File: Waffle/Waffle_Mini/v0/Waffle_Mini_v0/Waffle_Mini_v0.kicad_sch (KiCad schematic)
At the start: 17 parts, among them J1 cJTAG, U1 F2800154QRHBRQ1, U2 AP7375-33SA-7, X1 CSTNE20M0V530000R0

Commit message: Layout kinda done v0 waffle mini
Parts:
- removed J1: cJTAG, Connector_PinHeader_1.27mm:PinHeader_1x06_P1.27mm_Vertical_SMD_Pin1Left, symbol Connector_Generic:Conn_02x03_Odd_Even
- added J1: Conn_ARM_SWD_TagConnect_TC2030-NL, Connector:Tag-Connect_TC2030-IDC-NL_2x03_P1.27mm_Vertical, symbol Connector:Conn_ARM_SWD_TagConnect_TC2030-NL
- added J10, J11, J12, J13, J14, J15, J16, J17, J18, J19, J2, J20, J21, J22, J23, J24, J25, J26, J27, J28, J29, J3, J4, J5, J6, J7, J8, J9: Conn_01x01_Socket, ICDB_Waffle:ICDB_Castellated_Pad, symbol Connector:Conn_01x01_Socket
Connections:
- net +3.3V: now also J1.1 (VCC), J25.1 (Pin_1)
- net +VSW: now also J24.1 (Pin_1)
- net GND: now also J1.5 (GND), J15.1 (Pin_1), J16.1 (Pin_1), J26.1 (Pin_1), J27.1 (Pin_1), J28.1 (Pin_1), J29.1 (Pin_1)
- net JTAG_TCK: now also J1.4 (SWCLK)
- net JTAG_TMS: now also J1.2 (SWDIO)
- net XRSn: now also J1.3 (~{RESET})
- net at U1.12 (A4/C14): now also J10.1 (Pin_1)
- net at U1.13 (A10/C10_C8/A9_GPIO227_230): now also J11.1 (Pin_1)
- net at U1.14 (GPIO11): now also J12.1 (Pin_1)
- net at U1.15 (GPIO24): now also J13.1 (Pin_1)
- net at U1.17 (GPIO37_TDO): now also J14.1 (Pin_1)
- net at U1.2 (GPIO226_228_A6/C6): now also J2.1 (Pin_1)
- net at U1.26 (GPIO3): now also J17.1 (Pin_1)
- net at U1.27 (GPIO1): now also J18.1 (Pin_1)
- net at U1.28 (GPIO0): now also J19.1 (Pin_1)
- net at U1.29 (GPIO7): now also J20.1 (Pin_1)
- net at U1.3 (GPIO242_A3/C5): now also J3.1 (Pin_1)
- net at U1.30 (GPIO5): now also J21.1 (Pin_1)
- net at U1.31 (GPIO29): now also J22.1 (Pin_1)
- net at U1.32 (A16/C16_GPIO28): now also J23.1 (Pin_1)
- net at U1.4 (GPIO224_A2/C9): now also J4.1 (Pin_1)
- net at U1.5 (A15/C7_C4/A14): now also J5.1 (Pin_1)
- net at U1.6 (A11/C0_A5/C2): now also J6.1 (Pin_1)
- net at U1.7 (A0/C15/CMP1_DACL_A1): now also J7.1 (Pin_1)
- net at U1.8 (A12/C1_A7/C3): now also J8.1 (Pin_1)
- net at U1.9 (A8/C11): now also J9.1 (Pin_1)
- no-connect marks 0 -> 3
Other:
- moved on the sheet: R2, R3

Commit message: Curly added :)
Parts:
- added C11: 10n, Capacitor_SMD:C_0603_1608Metric, symbol Device:C_Small
- added R4: 4k7, Resistor_SMD:R_0603_1608Metric, symbol Device:R_Small_US
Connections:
- net +3.3V: now also R4.1
- net GND: now also C11.2
- net XRSn: now also C11.1, R4.2
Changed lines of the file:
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@@
   (junction (at 66.04 35.56) (diameter 0) (color 0 0 0 0)
+  )
+  (junction (at 21.59 123.19) (diameter 0) (color 0 0 0 0)
   )
   (junction (at 29.21 85.09) (diameter 0) (color 0 0 0 0)
@@
     (stroke (width 0) (type default))
   )
+  (wire (pts (xy 21.59 115.57) (xy 21.59 116.84))
+    (stroke (width 0) (type default))
+  )
   (wire (pts (xy 69.85 130.81) (xy 83.82 130.81))
     (stroke (width 0) (type default))
   )
-  (wire (pts (xy 26.67 123.19) (xy 34.29 123.19))
+  (wire (pts (xy 21.59 123.19) (xy 34.29 123.19))
     (stroke (width 0) (type default))
   )
@@
     (stroke (width 0) (type default))
   )
+  (wire (pts (xy 21.59 129.54) (xy 21.59 130.81))
+    (stroke (width 0) (type default))
+  )
   (wire (pts (xy 69.85 123.19) (xy 83.82 123.19))
     (stroke (width 0) (type default))
@@
     (stroke (width 0) (type default))
   )
+  (wire (pts (xy 21.59 123.19) (xy 21.59 124.46))
+    (stroke (width 0) (type default))
+  )
   (polyline (pts (xy 223.52 130.81) (xy 223.52 135.89))
     (stroke (width 0) (type default))
@@
   )
   (wire (pts (xy 69.85 144.78) (xy 83.82 144.78))
+    (stroke (width 0) (type default))
+  )
+  (wire (pts (xy 21.59 121.92) (xy 21.59 123.19))
     (stroke (width 0) (type default))
   )
@@
     )
   )
+  (symbol (lib_id "power:+3.3V") (at 21.59 115.57 0) (unit 1)
+    (in_bom yes) (on_board yes) (dnp no) (fields_autoplaced)
+    (property "Reference" "#PWR028" (at 21.59 119.38 0)
+      (effects (font (size 1.27 1.27)) hide)
+    )
+    (property "Value" "+3.3V" (at 21.59 110.49 0)
+      (effects (font (size 1.27 1.27)))
+    )
+    (property "Footprint" "" (at 21.59 115.57 0)
+      (effects (font (size 1.27 1.27)) hide)
+    )
+    (property "Datasheet" "" (at 21.59 115.57 0)
+      (effects (font (size 1.27 1.27)) hide)
+    )
+    (pin "1")
+    (instances
+      (project "Waffle_Mini_v0"
+        (path "/549e8335-6523-4521-9df7-6bd7c43d4ddf"
+          (reference "#PWR028") (unit 1)
+        )
+      )
+    )
+  )
   (symbol (lib_id "power:+3.3V") (at 29.21 78.74 0) (unit 1)
     (in_bom yes) (on_board yes) (dnp no) (fields_autoplaced)
@@
         (path "/549e8335-6523-4521-9df7-6bd7c43d4ddf"
           (reference "C7") (unit 1)
+        )
+      )
+    )
+  )
+  (symbol (lib_id "Device:C_Small") (at 21.59 127 0) (mirror y) (unit 1)
+    (in_bom yes) (on_board yes) (dnp no)
+    (property "Reference" "C11" (at 19.05 125.7363 0)
+      (effects (font (size 1.27 1.27)) (justify left))
+    )
+    (property "Value" "10n" (at 19.05 128.2763 0)
+      (effects (font (size 1.27 1.27)) (justify left))
+    )
+    (property "Footprint" "Capacitor_SMD:C_0603_1608Metric" (at 21.59 127 0)
+      (effects (font (size 1.27 1.27)) hide)
+    )
+    (property "Datasheet" "~" (at 21.59 127 0)
+      (effects (font (size 1.27 1.27)) hide)
+    )
+    (pin "1")
+    (pin "2")
+    (instances
+      (project "Waffle_Mini_v0"
+        (path "/549e8335-6523-4521-9df7-6bd7c43d4ddf"
+          (reference "C11") (unit 1)
         )
       )
@@
     )
   )
+  (symbol (lib_id "Device:R_Small_US") (at 21.59 119.38 0) (mirror y) (unit 1)
+    (in_bom yes) (on_board yes) (dnp no)
+    (property "Reference" "R4" (at 19.05 118.11 0)
+      (effects (font (size 1.27 1.27)) (justify left))
+    )
+    (property "Value" "4k7" (at 19.05 120.65 0)
+      (effects (font (size 1.27 1.27)) (justify left))
+    )
+    (property "Footprint" "Resistor_SMD:R_0603_1608Metric" (at 21.59 119.38 0)
+      (effects (font (size 1.27 1.27)) hide)
+    )
+    (property "Datasheet" "~" (at 21.59 119.38 0)
+      (effects (font (size 1.27 1.27)) hide)
+    )
+    (pin "1")
+    (pin "2")
+    (instances
+      (project "Waffle_Mini_v0"
+        (path "/549e8335-6523-4521-9df7-6bd7c43d4ddf"
+          (reference "R4") (unit 1)
+        )
+      )
+    )
+  )
   (symbol (lib_id "power:GND") (at 185.42 49.53 0) (unit 1)
     (in_bom yes) (on_board yes) (dnp no) (fields_autoplaced)
@@
         )
       )
+    )
+  )
+  (symbol (lib_id "power:GND") (at 21.59 130.81 0) (unit 1)
+    (in_bom yes) (on_board yes) (dnp no) (fields_autoplaced)
+    (property "Reference" "#PWR029" (at 21.59 137.16 0)
+      (effects (font (size 1.27 1.27)) hide)
+    )
+    (property "Value" "GND" (at 21.59 135.89 0)
+      (effects (font (size 1.27 1.27)))
+    )
+    (property "Footprint" "" (at 21.59 130.81 0)
+      (effects (font (size 1.27 1.27)) hide)
+    )
+    (property "Datasheet" "" (at 21.59 130.81 0)
+      (effects (font (size 1.27 1.27)) hide)
+    )
+    (pin "1")
+    (instances
+      (project "Waffle_Mini_v0"
+        (path "/549e8335-6523-4521-9df7-6bd7c43d4ddf"
+          (reference "#PWR029") (unit 1)
+        )
+      )

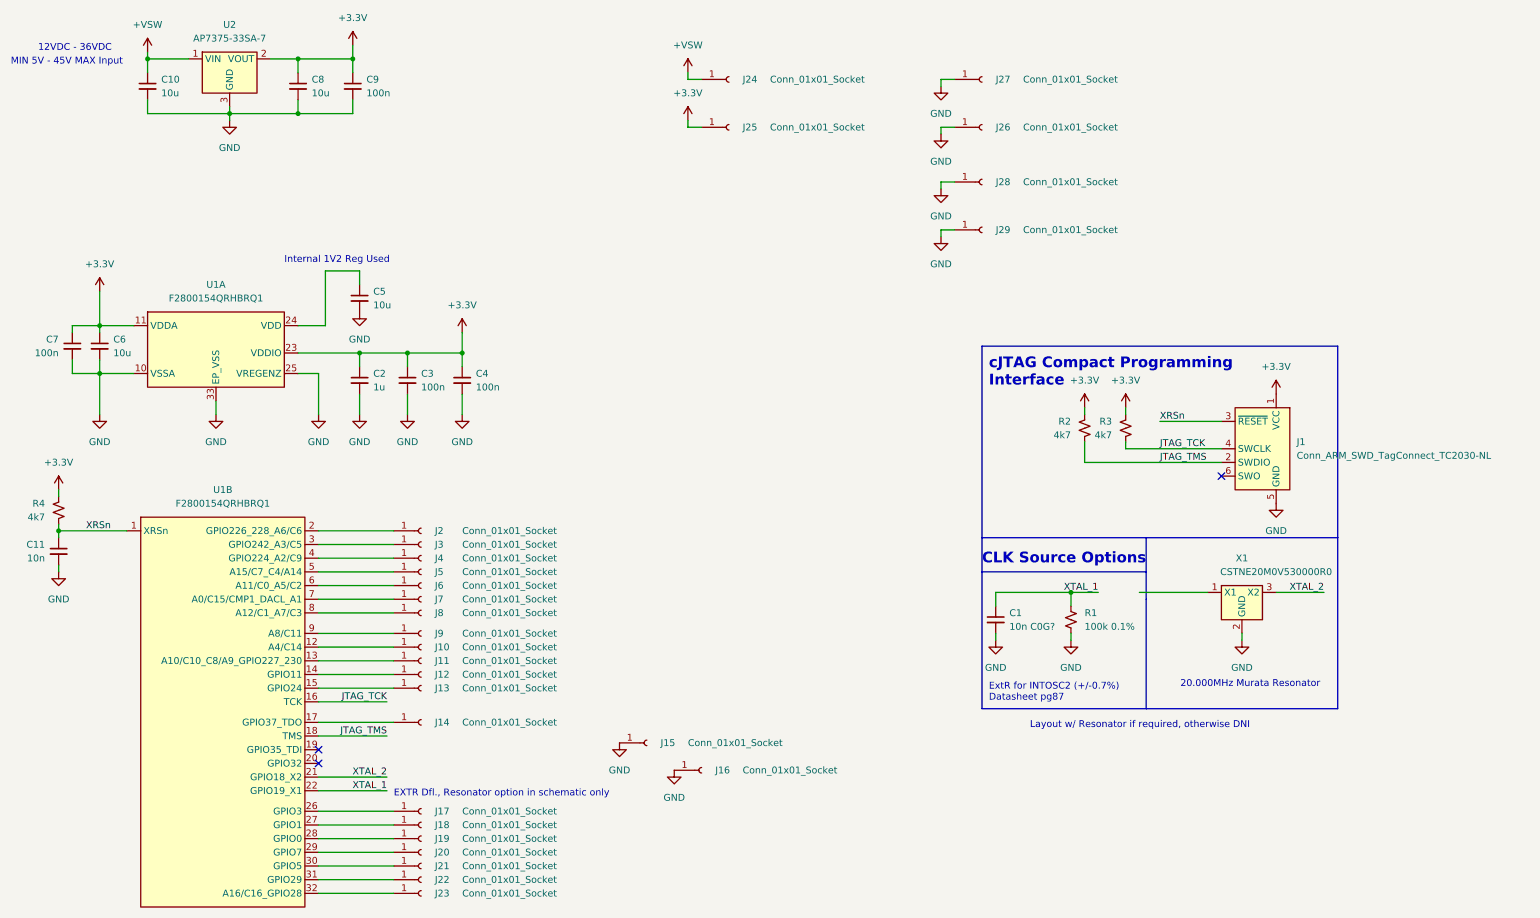
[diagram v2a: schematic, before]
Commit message: Blinky works on Curly :) Added CAN transceiver to Waffle
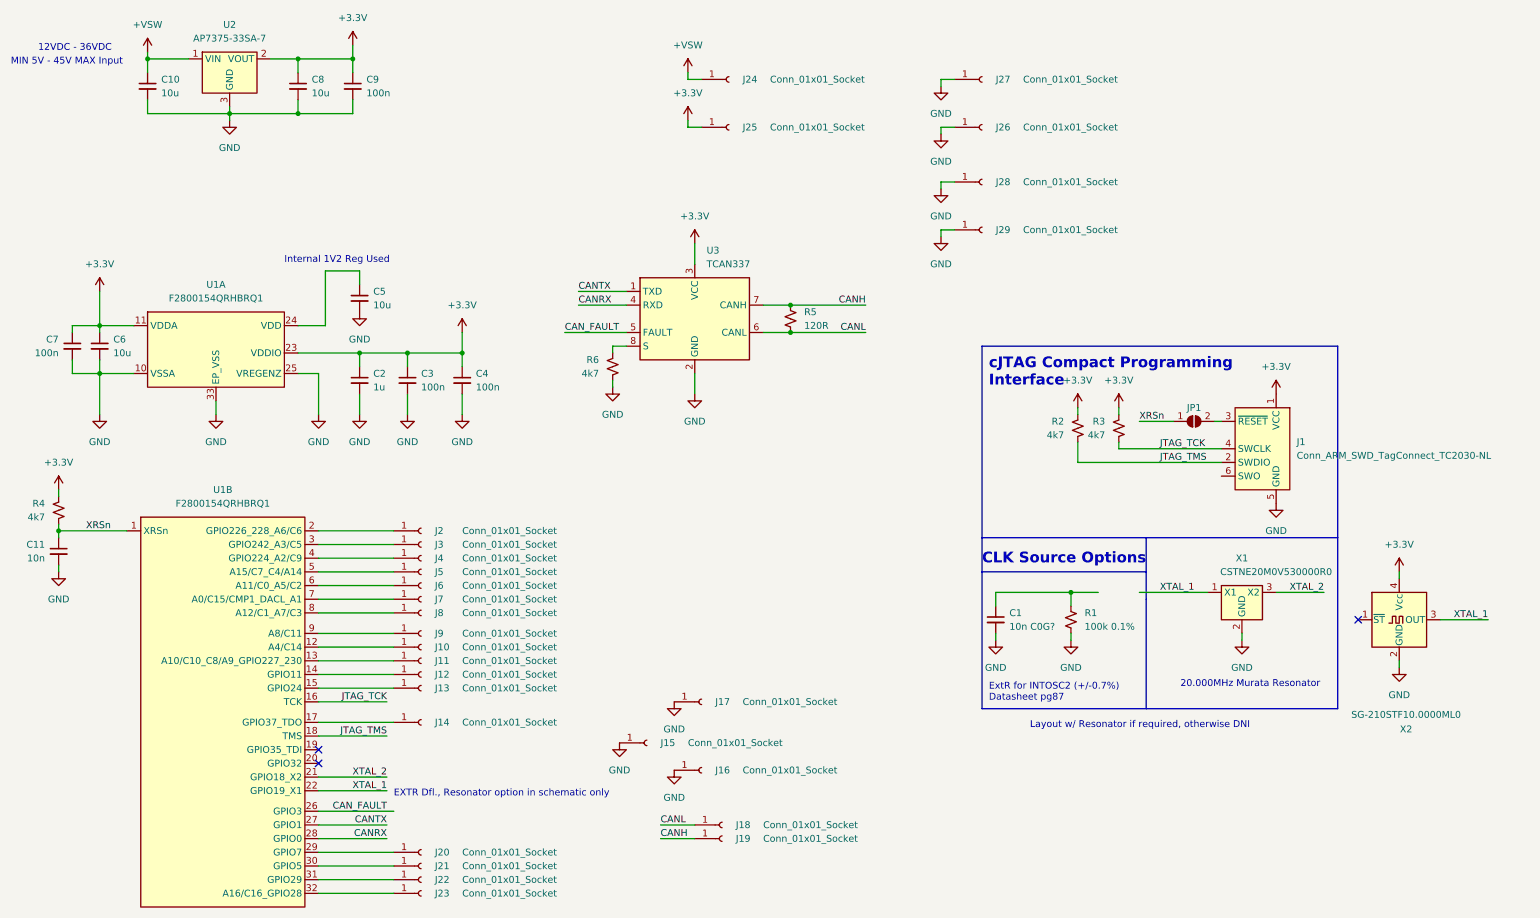
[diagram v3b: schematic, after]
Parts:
- added JP1: SolderJumper_2_Open, Jumper:SolderJumper-2_P1.3mm_Open_TrianglePad1.0x1.5mm, symbol Jumper:SolderJumper_2_Open
- added R5: 120R, Resistor_SMD:R_0805_2012Metric, symbol Device:R_Small_US
- added R6: 4k7, Resistor_SMD:R_0603_1608Metric, symbol Device:R_Small_US
- added U3: TCAN337, Package_TO_SOT_SMD:SOT-23-8, symbol Interface_CAN_LIN:TCAN337
- added X2: SG-210STF10.0000ML0, Oscillator:Oscillator_SMD_SeikoEpson_SG210-4Pin_2.5x2.0mm, symbol Oscillator:SG-210STF
- X1: footprint (none) -> ICDB_Waffle:CSTNE_Murata_Resonator
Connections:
- net +3.3V: now also U3.3 (VCC), X2.4 (Vcc)
- net GND: now also J17.1 (Pin_1), R6.2, U3.2 (GND), X2.2 (GND)
- net XRSn: now also JP1.1 (A); no longer J1.3 (~{RESET})
- net XTAL_1: now also X1.1 (X1), X2.3 (OUT); no longer C1.1, R1.1
- net CAN_FAULT: now reaches U1.26 (GPIO3)
- net CAN_FAULT: now also U3.5 (FAULT); no longer J17.1 (Pin_1)
- net CANL: now reaches J18.1 (Pin_1)
- net CANL: now also R5.2, U3.6 (CANL); no longer U1.27 (GPIO1)
- net CANH: now reaches J19.1 (Pin_1)
- net CANH: now also R5.1, U3.7 (CANH); no longer U1.28 (GPIO0)
- new net: J1.3 (~{RESET}), JP1.2 (B)
- new net: C1.1, R1.1
- new net: R6.1, U3.8 (S)
- new net CANRX: U1.28 (GPIO0), U3.4 (RXD)
- new net CANTX: U1.27 (GPIO1), U3.1 (TXD)
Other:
- moved on the sheet: J17, J18, J19, R2, R3
